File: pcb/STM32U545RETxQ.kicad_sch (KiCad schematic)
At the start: 19 parts, among them U3 STM32U545RETxQ

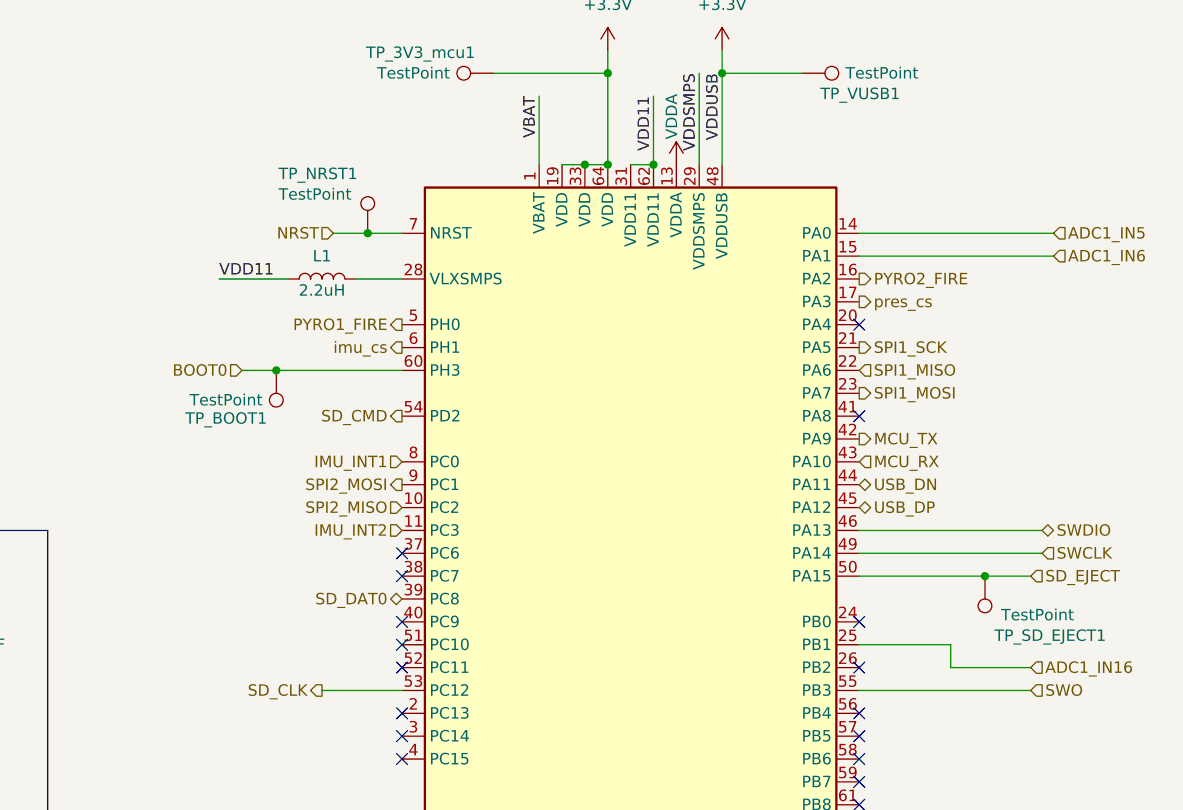
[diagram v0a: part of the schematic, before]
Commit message: Updated schematics and removed most test points
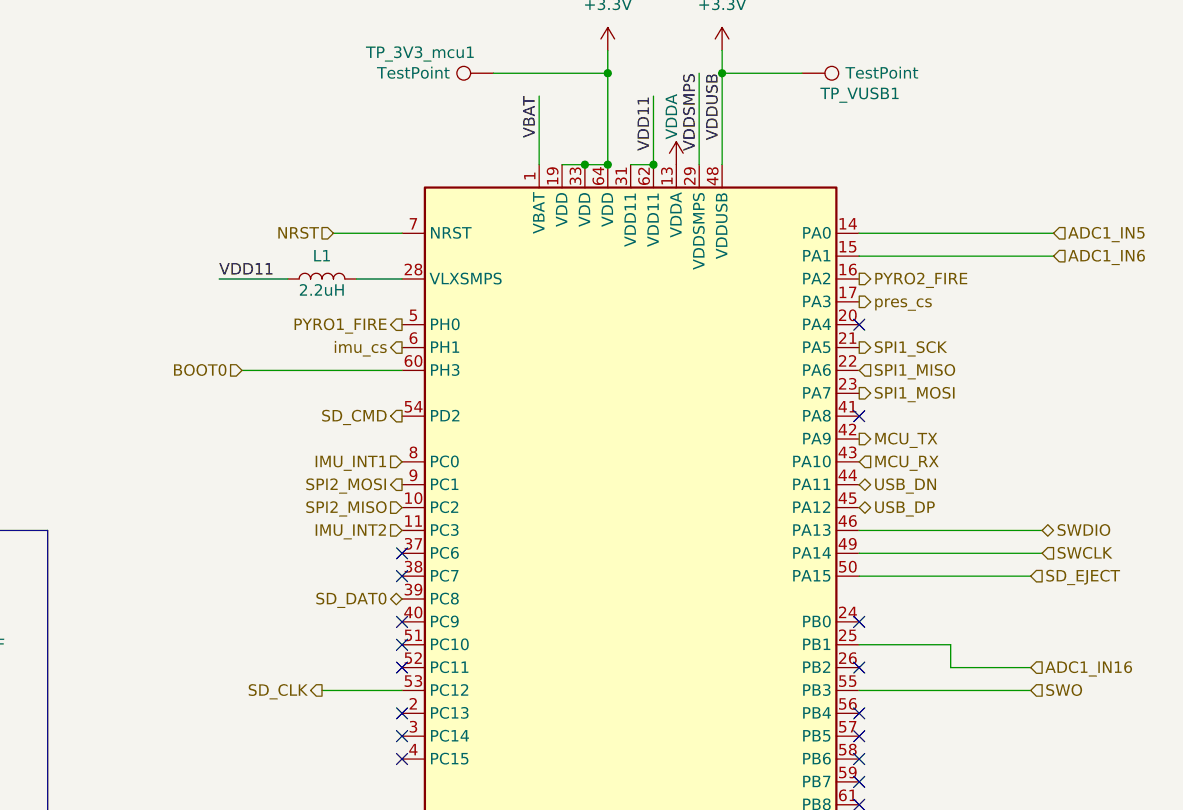
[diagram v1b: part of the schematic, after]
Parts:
- removed TP_BOOT1, TP_NRST1, TP_SD_EJECT1: TestPoint, TestPoint:TestPoint_Loop_D2.54mm_Drill1.5mm_Beaded, symbol Connector:TestPoint
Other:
- title: Ride-Along Module -> Control Module Rev2

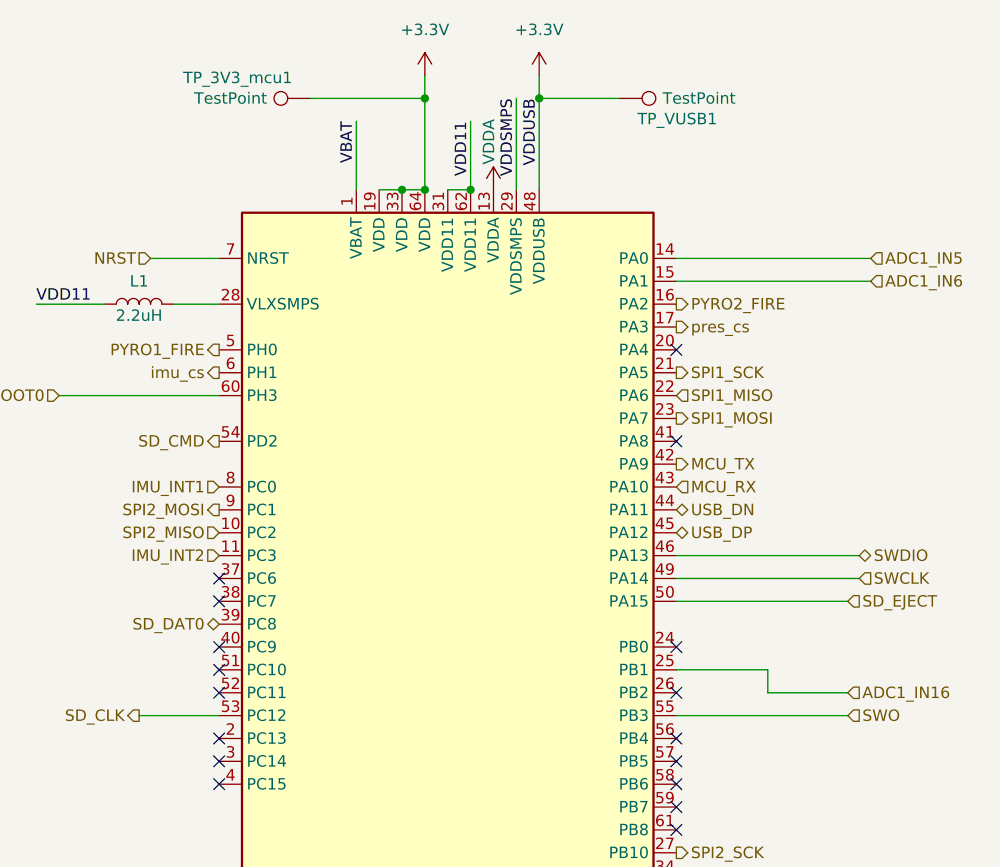
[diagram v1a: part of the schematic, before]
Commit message: Updated Board layout, finalized dimensions
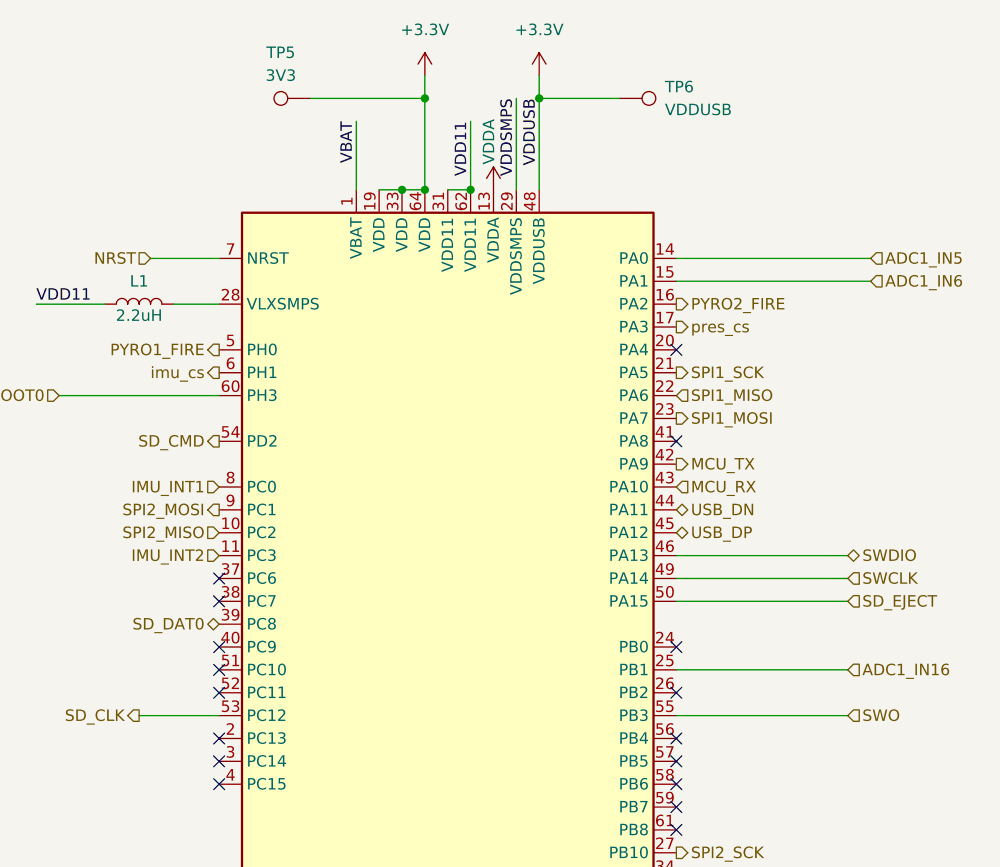
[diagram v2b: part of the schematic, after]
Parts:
- removed TP_3V3_mcu1, TP_VUSB1: TestPoint, TestPoint:TestPoint_Loop_D2.54mm_Drill1.5mm_Beaded, symbol Connector:TestPoint
- added TP5: 3V3, TestPoint:TestPoint_Pad_D1.5mm, symbol Connector:TestPoint
- added TP6: VDDUSB, TestPoint:TestPoint_Pad_D1.5mm, symbol Connector:TestPoint
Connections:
- net +3.3V: now also TP5.1, TP6.1
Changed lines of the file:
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@@
 	(wire
 		(pts
-			(xy 184.15 104.14) (xy 194.31 104.14)
+			(xy 184.15 104.14) (xy 203.2 104.14)
 		)
 		(stroke
@@
 	(wire
 		(pts
-			(xy 184.15 93.98) (xy 204.47 93.98)
+			(xy 184.15 93.98) (xy 203.2 93.98)
 		)
 		(stroke
@@
 	(wire
 		(pts
-			(xy 194.31 106.68) (xy 203.2 106.68)
-		)
-		(stroke
-			(width 0)
-			(type default)
-		)
-	)
-	(wire
-		(pts
 			(xy 168.91 38.1) (xy 168.91 40.64)
 		)
@@
 	(wire
 		(pts
-			(xy 184.15 91.44) (xy 204.47 91.44)
+			(xy 184.15 91.44) (xy 203.2 91.44)
 		)
 		(stroke
@@
 		(pts
 			(xy 156.21 38.1) (xy 156.21 40.64)
-		)
-		(stroke
-			(width 0)
-			(type default)
-		)
-	)
-	(wire
-		(pts
-			(xy 194.31 104.14) (xy 194.31 106.68)
 		)
 		(stroke
@@
 	(hierarchical_label "ADC1_IN16"
 		(shape input)
-		(at 203.2 106.68 0)
+		(at 203.2 104.14 0)
 		(effects
 			(font
@@
 	(hierarchical_label "SWCLK"
 		(shape input)
-		(at 204.47 93.98 0)
+		(at 203.2 93.98 0)
 		(effects
 			(font
@@
 	(hierarchical_label "SWDIO"
 		(shape bidirectional)
-		(at 204.47 91.44 0)
+		(at 203.2 91.44 0)
 		(effects
 			(font
@@
 	)
 	(symbol
+		(lib_id "Connector:TestPoint")
+		(at 143.51 40.64 90)
+		(unit 1)
+		(exclude_from_sim no)
+		(in_bom yes)
+		(on_board yes)
+		(dnp no)
+		(fields_autoplaced yes)
+		(property "Reference" "TP5"
+			(at 140.208 35.56 90)
+			(effects
+				(font
+					(size 1.27 1.27)
+				)
+			)
+		)
+		(property "Value" "3V3"
+			(at 140.208 38.1 90)
+			(effects
+				(font
+					(size 1.27 1.27)
+				)
+			)
+		)
+		(property "Footprint" "TestPoint:TestPoint_Pad_D1.5mm"
+			(at 143.51 35.56 0)
+			(effects
+				(font
+					(size 1.27 1.27)
+				)
+				(hide yes)
+			)
+		)
+		(property "Datasheet" "~"
+			(at 143.51 35.56 0)
+			(effects
+				(font
+					(size 1.27 1.27)
+				)
+				(hide yes)
+			)
+		)
+		(property "Description" "test point"
+			(at 143.51 40.64 0)
+			(effects
+				(font
+					(size 1.27 1.27)
+				)
+				(hide yes)
+			)
+		)
+		(pin "1"
+		)
+		(instances
+			(project "control-module"
+				(path "/ba7b4294-8d75-4b9e-892f-fb52727887ec/646bb59c-dea9-4304-8415-d4c1819f029f"
+					(reference "TP5")
+					(unit 1)
+				)
+			)
+		)
+	)
+	(symbol
 		(lib_id "power:GNDD")
 		(at 161.29 142.24 0)
@@
 				(path "/ba7b4294-8d75-4b9e-892f-fb52727887ec/646bb59c-dea9-4304-8415-d4c1819f029f"
 					(reference "#PWR041")
-					(unit 1)
-				)
-			)
-		)
-	)
-	(symbol
-		(lib_id "Connector:TestPoint")
-		(at 143.51 40.64 90)
-		(unit 1)
-		(exclude_from_sim no)
-		(in_bom yes)
-		(on_board yes)
-		(dnp no)
-		(property "Reference" "TP_3V3_mcu1"
-			(at 141.478 38.354 90)
-			(effects
-				(font
-					(size 1.27 1.27)
-				)
-				(justify left)
-			)
-		)
-		(property "Value" "TestPoint"
-			(at 138.684 40.64 90)
-			(effects
-				(font
-					(size 1.27 1.27)
-				)
-				(justify left)
-			)
-		)
-		(property "Footprint" "TestPoint:TestPoint_Loop_D2.54mm_Drill1.5mm_Beaded"
-			(at 143.51 35.56 0)
-			(effects
-				(font
-					(size 1.27 1.27)
-				)
-				(hide yes)
-			)
-		)
-		(property "Datasheet" "https://www.keyelco.com/userAssets/file/M65p56.pdf"
-			(at 143.51 35.56 0)
-			(effects
-				(font
-					(size 1.27 1.27)
-				)
-				(hide yes)
-			)
-		)
-		(property "Description" "test point"
-			(at 143.51 40.64 0)
-			(effects
-				(font
-					(size 1.27 1.27)
-				)
-				(hide yes)
-			)
-		)
-		(property "Purchase" "https://www.digikey.com/en/products/detail/keystone-electronics/5000/255326"
-			(at 143.51 40.64 0)
-			(effects
-				(font
-					(size 1.27 1.27)
-				)
-				(hide yes)
-			)
-		)
-		(pin "1"
-		)
-		(instances
-			(project "control-module"
-				(path "/ba7b4294-8d75-4b9e-892f-fb52727887ec/646bb59c-dea9-4304-8415-d4c1819f029f"
-					(reference "TP_3V3_mcu1")
 					(unit 1)
 				)
@@
 	)
 	(symbol
-		(lib_id "Connector:TestPoint")
-		(at 177.8 40.64 270)
-		(unit 1)
-		(exclude_from_sim no)
-		(in_bom yes)
-		(on_board yes)
-		(dnp no)
-		(property "Reference" "TP_VUSB1"
-			(at 179.832 42.926 90)
-			(effects
-				(font
-					(size 1.27 1.27)
-				)
-				(justify left)
-			)
-		)
-		(property "Value" "TestPoint"
-			(at 182.626 40.64 90)
-			(effects
-				(font
-					(size 1.27 1.27)
-				)
-				(justify left)
-			)
-		)
-		(property "Footprint" "TestPoint:TestPoint_Loop_D2.54mm_Drill1.5mm_Beaded"
-			(at 177.8 45.72 0)
-			(effects
-				(font
-					(size 1.27 1.27)
-				)
-				(hide yes)
-			)
-		)
-		(property "Datasheet" "https://www.keyelco.com/userAssets/file/M65p56.pdf"
-			(at 177.8 45.72 0)
-			(effects
-				(font
-					(size 1.27 1.27)
-				)
-				(hide yes)
-			)
-		)
-		(property "Description" "test point"
-			(at 177.8 40.64 0)
-			(effects
-				(font
-					(size 1.27 1.27)
-				)
-				(hide yes)
-			)
-		)
-		(property "Purchase" "https://www.digikey.com/en/products/detail/keystone-electronics/5000/255326"
-			(at 177.8 40.64 0)
-			(effects
-				(font
-					(size 1.27 1.27)
-				)
-				(hide yes)
-			)
-		)
-		(pin "1"
-		)
-		(instances
-			(project "control-module"
-				(path "/ba7b4294-8d75-4b9e-892f-fb52727887ec/646bb59c-dea9-4304-8415-d4c1819f029f"
-					(reference "TP_VUSB1")
-					(unit 1)
-				)
-			)
-		)
-	)
-	(symbol
 		(lib_id "Device:C")
 		(at 67.31 151.13 0)
@@
 					(unit 1)
 				)
+			)
+		)
+	)
+	(symbol
+		(lib_id "Connector:TestPoint")
+		(at 177.8 40.64 270)
+		(unit 1)
+		(exclude_from_sim no)
+		(in_bom yes)
+		(on_board yes)
+		(dnp no)
+		(fields_autoplaced yes)
+		(property "Reference" "TP6"
+			(at 182.88 39.3699 90)
+			(effects
+				(font
+					(size 1.27 1.27)
+				)
+				(justify left)
+			)
+		)
+		(property "Value" "VDDUSB"
+			(at 182.88 41.9099 90)
+			(effects
+				(font
+					(size 1.27 1.27)
+				)
+				(justify left)
+			)
+		)
+		(property "Footprint" "TestPoint:TestPoint_Pad_D1.5mm"
+			(at 177.8 45.72 0)
+			(effects
+				(font
+					(size 1.27 1.27)
+				)
+				(hide yes)
+			)
+		)
+		(property "Datasheet" "~"
+			(at 177.8 45.72 0)
+			(effects
+				(font
+					(size 1.27 1.27)
+				)
+				(hide yes)
+			)
+		)
+		(property "Description" "test point"
+			(at 177.8 40.64 0)
+			(effects
+				(font
+					(size 1.27 1.27)
+				)
+				(hide yes)
+			)
+		)
+		(pin "1"
+		)
+		(instances
+			(project "control-module"
+				(path "/ba7b4294-8d75-4b9e-892f-fb52727887ec/646bb59c-dea9-4304-8415-d4c1819f029f"
+					(reference "TP6")
+					(unit 1)
+				)

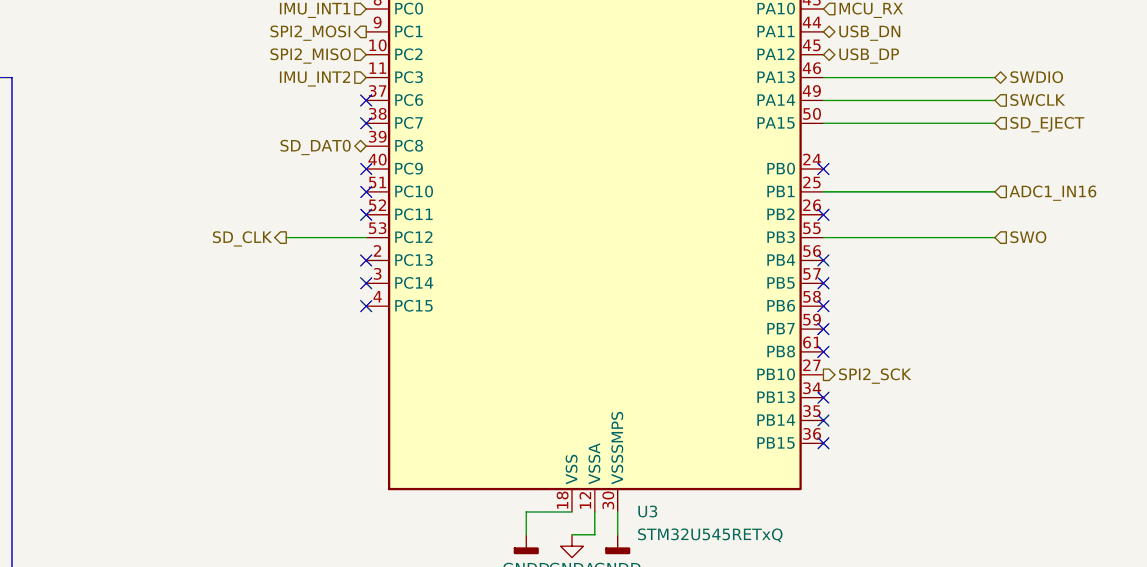
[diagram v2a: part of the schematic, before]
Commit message: Updated Board size and layout
Full Layout of Rev 2 board, without RF shield and other updates.
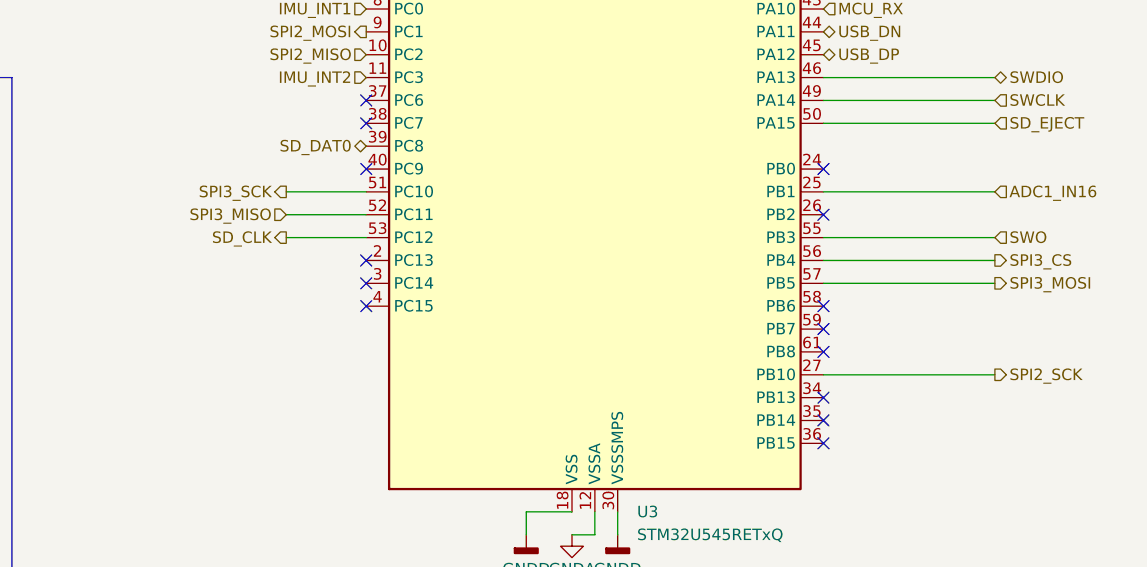
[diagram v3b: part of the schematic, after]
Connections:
- net SPI3_SCK: now reaches U3.51 (PC10)
- net SPI3_MISO: now reaches U3.52 (PC11)
- net SPI3_CS: now reaches U3.56 (PB4)
- net SPI3_MOSI: now reaches U3.57 (PB5)
- no-connect marks 20 -> 16
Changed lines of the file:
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@@
-	)
-	(no_connect
-		(at 184.15 111.76)
-	)
-	(no_connect
-		(at 133.35 106.68)
 	)
 	(no_connect
@@
 	)
 	(no_connect
-		(at 184.15 114.3)
-	)
-	(no_connect
 		(at 184.15 119.38)
 	)
@@
 	)
 	(no_connect
-		(at 133.35 104.14)
-	)
-	(no_connect
 		(at 133.35 93.98)
 	)
@@
 	(wire
 		(pts
+			(xy 203.2 124.46) (xy 184.15 124.46)
+		)
+		(stroke
+			(width 0)
+			(type default)
+		)
+	)
+	(wire
+		(pts
 			(xy 54.61 124.46) (xy 67.31 124.46)
 		)
@@
 	(wire
 		(pts
+			(xy 184.15 111.76) (xy 203.2 111.76)
+		)
+		(stroke
+			(width 0)
+			(type default)
+		)
+	)
+	(wire
+		(pts
 			(xy 184.15 104.14) (xy 203.2 104.14)
 		)
@@
 	(wire
 		(pts
+			(xy 124.46 104.14) (xy 133.35 104.14)
+		)
+		(stroke
+			(width 0)
+			(type default)
+		)
+	)
+	(wire
+		(pts
+			(xy 184.15 114.3) (xy 203.2 114.3)
+		)
+		(stroke
+			(width 0)
+			(type default)
+		)
+	)
+	(wire
+		(pts
 			(xy 151.13 139.7) (xy 156.21 139.7)
 		)
@@
 		(pts
 			(xy 148.59 43.18) (xy 148.59 50.8)
+		)
+		(stroke
+			(width 0)
+			(type default)
+		)
+	)
+	(wire
+		(pts
+			(xy 124.46 106.68) (xy 133.35 106.68)
 		)
 		(stroke
@@
 		)
 	)
+	(hierarchical_label "SPI3_MISO"
+		(shape input)
+		(at 124.46 106.68 180)
+		(effects
+			(font
+				(size 1.27 1.27)
+			)
+			(justify right)
+		)
+	)
 	(hierarchical_label "SPI1_MOSI"
 		(shape output)
@@
 	(hierarchical_label "SPI2_SCK"
 		(shape output)
-		(at 184.15 124.46 0)
+		(at 203.2 124.46 0)
 		(effects
 			(font
@@
 		)
 	)
+	(hierarchical_label "SPI3_CS"
+		(shape output)
+		(at 203.2 111.76 0)
+		(effects
+			(font
+				(size 1.27 1.27)
+			)
+			(justify left)
+		)
+	)
 	(hierarchical_label "ADC1_IN6"
 		(shape input)
@@
 		)
 	)
+	(hierarchical_label "SPI3_SCK"
+		(shape output)
+		(at 124.46 104.14 180)
+		(effects
+			(font
+				(size 1.27 1.27)
+			)
+			(justify right)
+		)
+	)
+	(hierarchical_label "SPI3_MOSI"
+		(shape output)
+		(at 203.2 114.3 0)
+		(effects
+			(font
+				(size 1.27 1.27)
+			)
+			(justify left)
+		)
+	)
